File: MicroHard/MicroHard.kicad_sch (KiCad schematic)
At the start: 0 parts

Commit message: feat: added jumper
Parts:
- added JP1, JP2, JP3, JP4: Jumper_2_Bridged, symbol Jumper:Jumper_2_Bridged
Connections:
- net +1.0V: now also JP1.2 (B)
- net +1.8V: now also JP2.2 (B)
- net +3.3V: now also JP3.2 (B)
- net +3.3VA: now also JP4.2 (B)
- new net Power Supply/+1.0V: JP1.1 (A)
- new net Power Supply/+1.8V: JP2.1 (A)
- new net Power Supply/+3.3V: JP3.1 (A)
- new net Power Supply/+3.3VA: JP4.1 (A)

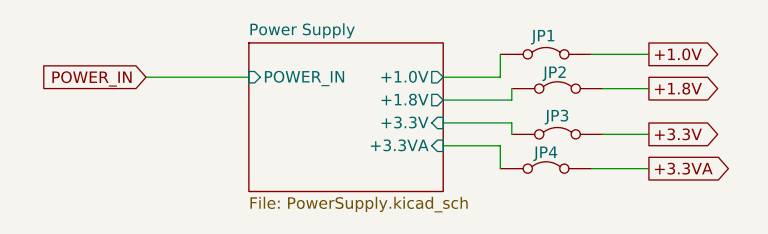
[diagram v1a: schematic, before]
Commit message: fix: powersupply passes ERV
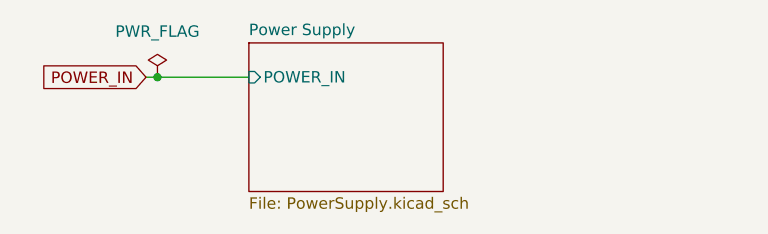
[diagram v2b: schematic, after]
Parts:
- removed JP1, JP2, JP3, JP4: Jumper_2_Bridged, symbol Jumper:Jumper_2_Bridged
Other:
- sheet Power Supply ports: added none; removed +1.0V, +1.8V, +3.3V, +3.3VA

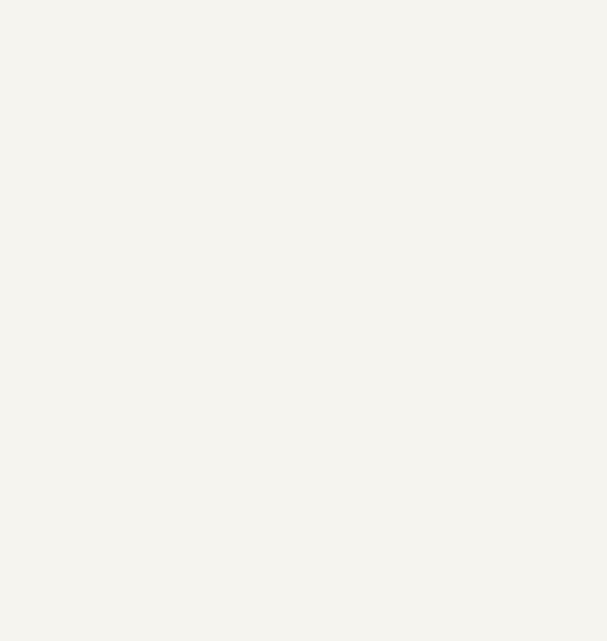
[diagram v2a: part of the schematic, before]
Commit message: Add mcu symbol and footprint
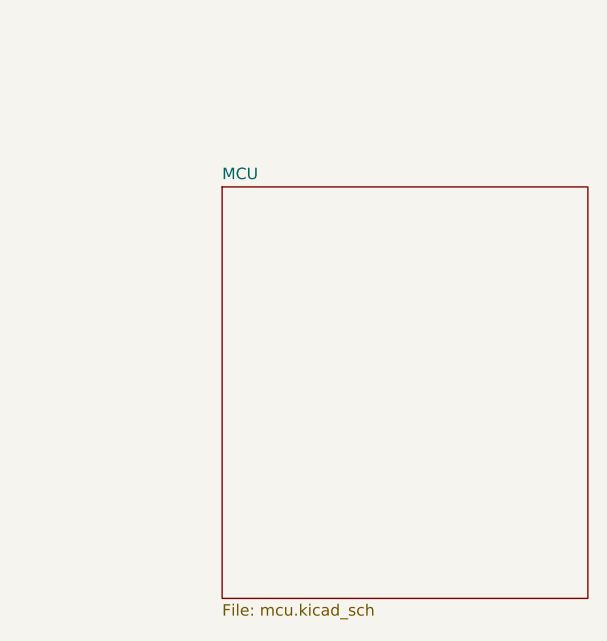
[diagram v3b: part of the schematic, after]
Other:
- added sheet MCU (mcu.kicad_sch)
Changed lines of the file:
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@@
+	)
+	(sheet
+		(at 116.84 76.2)
+		(size 40.64 45.72)
+		(fields_autoplaced yes)
+		(stroke
+			(width 0.1524)
+			(type solid)
+		)
+		(fill
+			(color 0 0 0 0.0000)
+		)
+		(property "Sheetname" "MCU"
+			(at 116.84 75.4884 0)
+			(effects
+				(font
+					(size 1.27 1.27)
+				)
+				(justify left bottom)
+			)
+		)
+		(property "Sheetfile" "mcu.kicad_sch"
+			(at 116.84 122.5046 0)
+			(effects
+				(font
+					(size 1.27 1.27)
+				)
+				(justify left top)
+			)
+		)
+		(instances
+			(project "MicroHard"
+				(path "/578bd531-a491-4b15-a479-460d159ffc14"
+					(page "3")
+				)
+			)
+		)
 	)
 	(sheet
